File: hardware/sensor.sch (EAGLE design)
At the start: 39 parts, among them IC1 BN055, IC2 BME280, J1 MICRO_USB_B_HIROSE_ZX62-B-5PA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, SW1 TVAF06-A020B-R, U2 NJM12888F, X1 FA-238

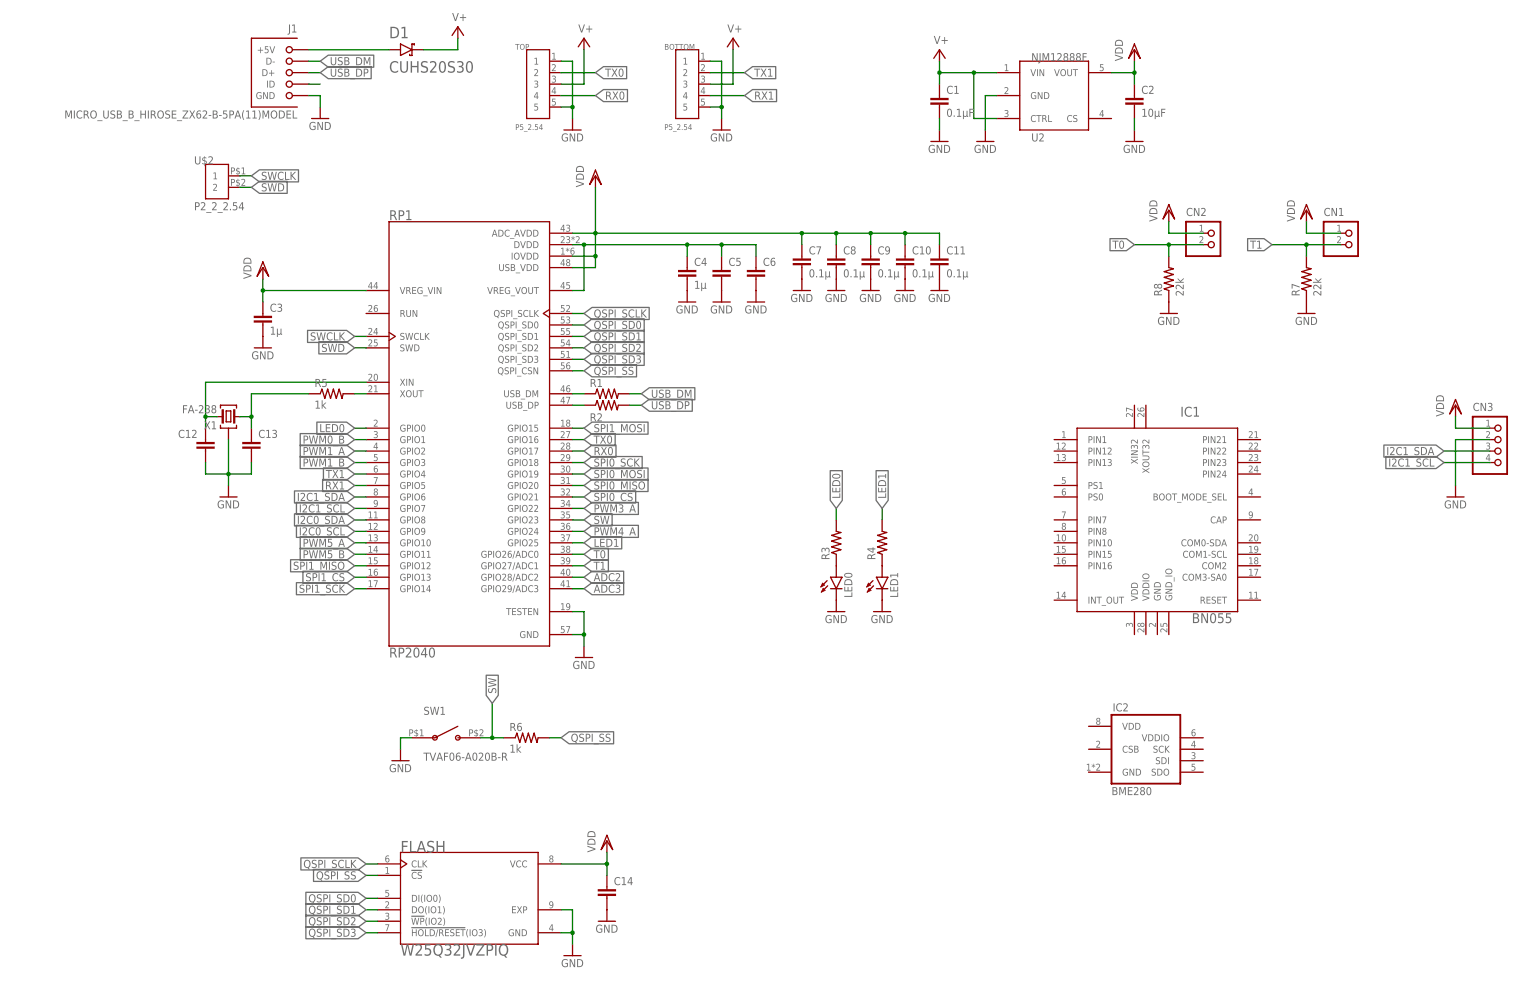
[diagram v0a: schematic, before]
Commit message: センサーの基盤完了しました。エラー処理とか諸々終わってないので年末年始で頑張ります。抵抗値とかなにも入力してなかったのでしばらくかかりそうです。
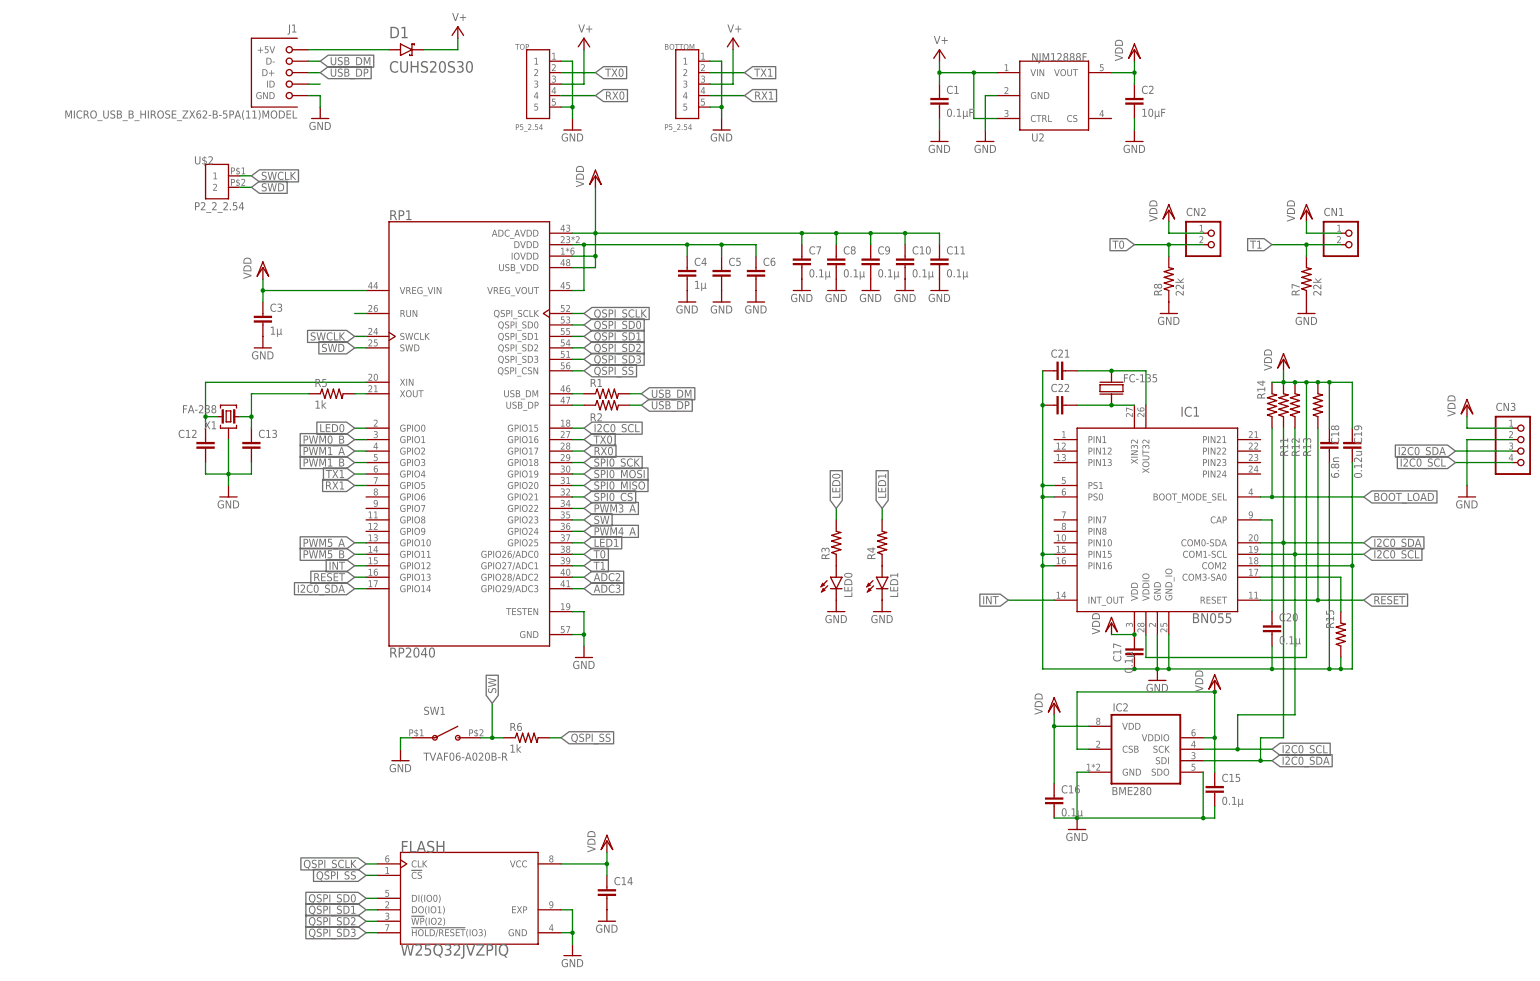
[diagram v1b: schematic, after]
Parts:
- added C15, C16, C17, C20: 0.1µ, rcl:C-EUC0402
- added C18: 6.8n, rcl:C-EUC0402
- added C19: 0.12u, rcl:C-EUC0402
- added C21, C22: (no value), rcl:C-EUC0402
- added FC-135: FC-135, tere:FC-135
- added R11, R12, R13, R14, R15: (no value), rcl:R-US_R0402
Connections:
- removed net I2C1_SCL: CN3.4, RP1.GPIO7
- removed net I2C1_SDA: CN3.3, RP1.GPIO6
- removed net SPI1_CS: RP1.GPIO13
- removed net SPI1_MISO: RP1.GPIO12
- removed net SPI1_MOSI: RP1.GPIO15
- removed net SPI1_SCK: RP1.GPIO14
- new net BOOT_LOAD: IC1.BOOT_MODE_SEL, R14.1
- new net INT: IC1.INT_OUT, RP1.GPIO12
- new net N$1: C20.1, IC1.CAP
- new net N$10: IC1.COM3-SA0, R15.2
- new net N$15: RP1.RUN
- new net N$3: C22.2, FC-135.P$2, IC1.XIN32
- new net N$4: C21.2, FC-135.P$1, IC1.XOUT32
- new net RESET: IC1.RESET, R13.1, RP1.GPIO13
- net GND: now also C15.2, C16.2, C17.2, C18.2, C19.2, C20.2, C21.1, C22.1, IC1.COM2, IC1.GND, IC1.GND_IO, IC1.PIN15, IC1.PIN16, IC1.PS0, IC1.PS1, IC2.GND, IC2.SDO, R15.1
- net I2C0_SCL: now also CN3.4, IC1.COM1-SCL, IC2.SCK, R12.1, RP1.GPIO15; no longer RP1.GPIO9
- net I2C0_SDA: now also CN3.3, IC1.COM0-SDA, IC2.SDI, R11.1, RP1.GPIO14; no longer RP1.GPIO8
- net VDD: now also C15.1, C16.1, C17.1, C18.1, C19.1, IC1.VDD, IC1.VDDIO, IC2.CSB, IC2.VDD, IC2.VDDIO, R11.2, R12.2, R13.2, R14.2
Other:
- moved on the sheet: CN3

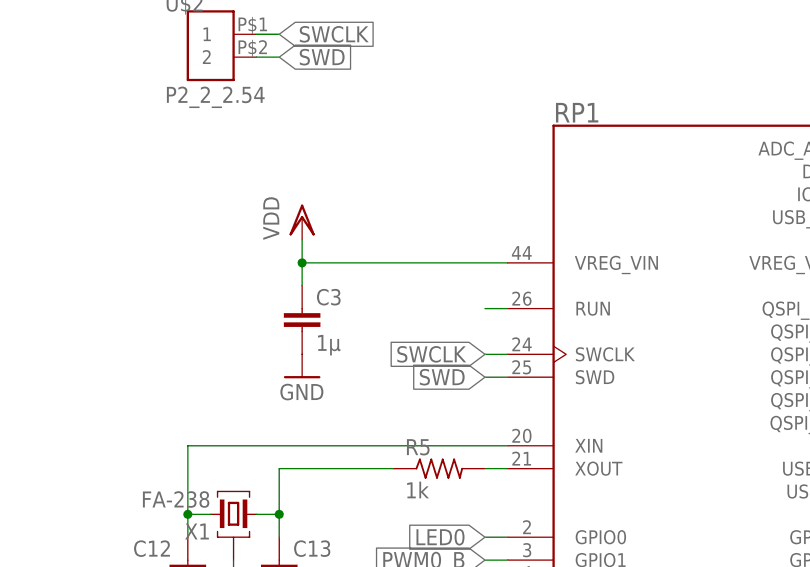
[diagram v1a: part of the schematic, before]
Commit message: べたGND前です。esp32のschはノータッチなのでここに上がってないです。よろしくお願いします。
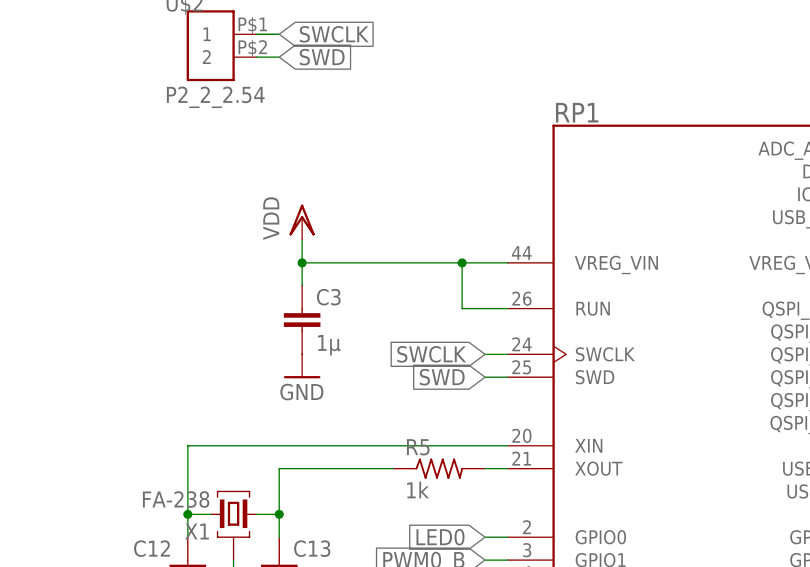
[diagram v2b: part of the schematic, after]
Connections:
- removed net N$15: RP1.RUN
- net VDD: now also RP1.RUN
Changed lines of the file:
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@@
 <segment>
 <pinref part="RP1" gate="G$1" pin="VREG_VIN"/>
-<wire x1="33.02" y1="127" x2="10.16" y2="127" width="0.1524" layer="91"/>
+<wire x1="33.02" y1="127" x2="27.94" y2="127" width="0.1524" layer="91"/>
 <pinref part="C3" gate="G$1" pin="1"/>
+<wire x1="27.94" y1="127" x2="10.16" y2="127" width="0.1524" layer="91"/>
 <wire x1="10.16" y1="127" x2="10.16" y2="124.46" width="0.1524" layer="91"/>
 <wire x1="10.16" y1="127" x2="10.16" y2="129.54" width="0.1524" layer="91"/>
 <junction x="10.16" y="127"/>
 <pinref part="VDD8" gate="G$1" pin="VDD"/>
+<pinref part="RP1" gate="G$1" pin="RUN"/>
+<wire x1="33.02" y1="121.92" x2="27.94" y2="121.92" width="0.1524" layer="91"/>
+<wire x1="27.94" y1="121.92" x2="27.94" y2="127" width="0.1524" layer="91"/>
+<junction x="27.94" y="127"/>
 </segment>
 <segment>
@@
 </segment>
 </net>
-<net name="N$15" class="0">
-<segment>
-<pinref part="RP1" gate="G$1" pin="RUN"/>
-<wire x1="33.02" y1="121.92" x2="30.48" y2="121.92" width="0.1524" layer="91"/>
-</segment>
-</net>

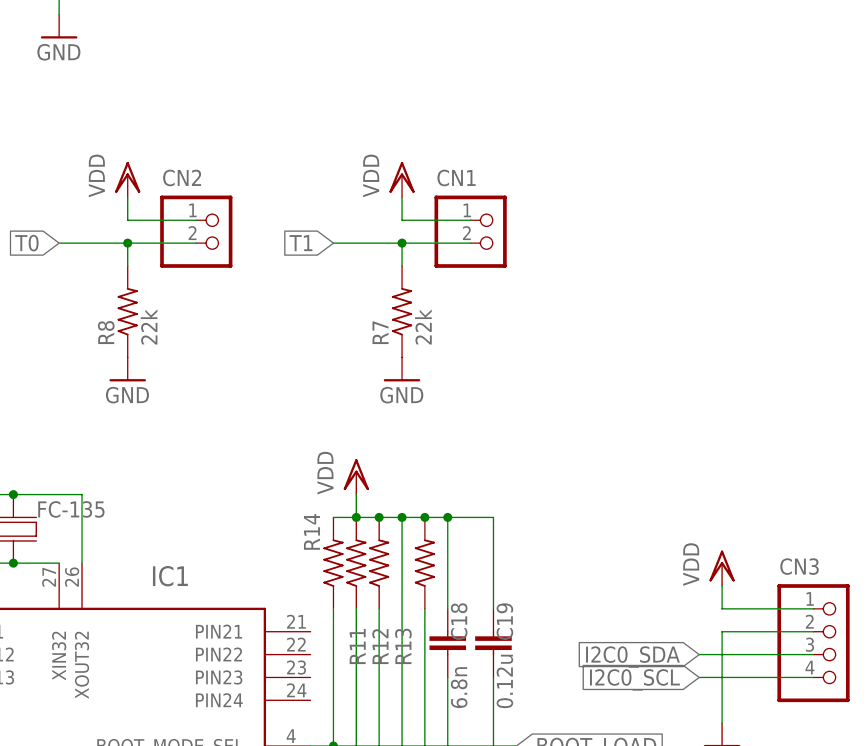
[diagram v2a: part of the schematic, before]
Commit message: シルクを調整
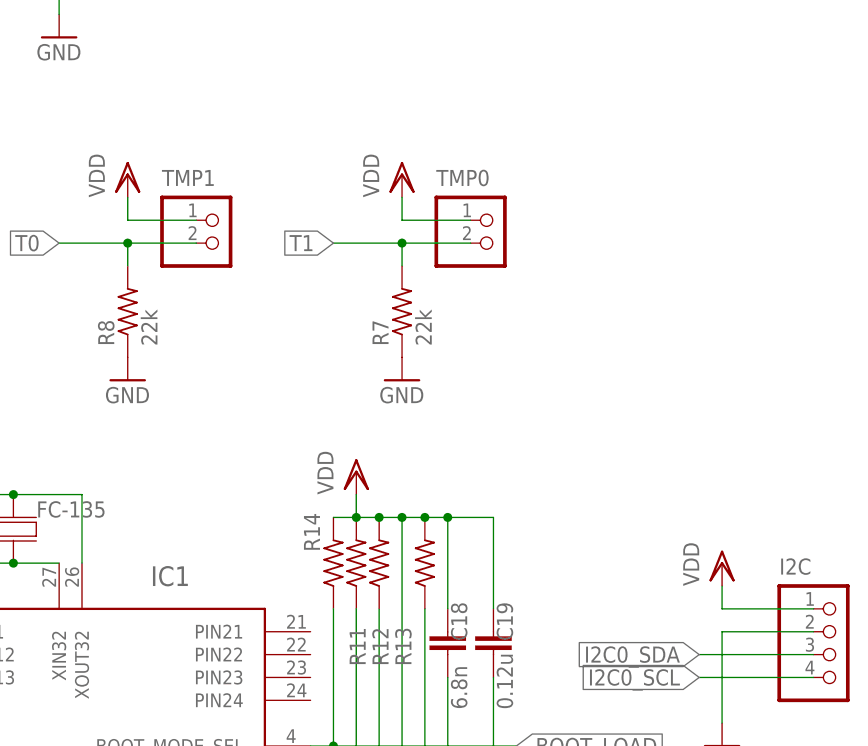
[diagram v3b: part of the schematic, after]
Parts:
- renumbered CN1 to TMP0, CN2 to TMP1, CN3 to I2C
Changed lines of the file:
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@@
 <part name="R7" library="rcl" library_urn="urn:adsk.eagle:library:334" deviceset="R-US_" device="R0402" package3d_urn="urn:adsk.eagle:package:23547/3" value="22k"/>
 <part name="GND1" library="supply1" library_urn="urn:adsk.eagle:library:371" deviceset="GND" device=""/>
-<part name="CN1" library="jst-ph" deviceset="S2B-PH-*" device="K-S"/>
+<part name="TMP0" library="jst-ph" deviceset="S2B-PH-*" device="K-S"/>
 <part name="VDD1" library="supply1" library_urn="urn:adsk.eagle:library:371" deviceset="VDD" device=""/>
 <part name="R8" library="rcl" library_urn="urn:adsk.eagle:library:334" deviceset="R-US_" device="R0402" package3d_urn="urn:adsk.eagle:package:23547/3" value="22k"/>
 <part name="GND2" library="supply1" library_urn="urn:adsk.eagle:library:371" deviceset="GND" device=""/>
-<part name="CN2" library="jst-ph" deviceset="S2B-PH-*" device="K-S"/>
+<part name="TMP1" library="jst-ph" deviceset="S2B-PH-*" device="K-S"/>
 <part name="VDD2" library="supply1" library_urn="urn:adsk.eagle:library:371" deviceset="VDD" device=""/>
-<part name="CN3" library="jst-ph" deviceset="B4B-PH-*" device="K-S"/>
+<part name="I2C" library="jst-ph" deviceset="B4B-PH-*" device="K-S"/>
 <part name="GND3" library="supply1" library_urn="urn:adsk.eagle:library:371" deviceset="GND" device=""/>
 <part name="VDD3" library="supply1" library_urn="urn:adsk.eagle:library:371" deviceset="VDD" device=""/>
@@
 <attribute name="VALUE" x="238.76" y="119.38" size="1.778" layer="96"/>
 </instance>
-<instance part="CN1" gate="G$1" x="248.92" y="139.7" smashed="yes">
+<instance part="TMP0" gate="G$1" x="248.92" y="139.7" smashed="yes">
 <attribute name="NAME" x="245.11" y="143.51" size="1.778" layer="95"/>
 <attribute name="VALUE" x="245.11" y="132.08" size="1.778" layer="96"/>
@@
 <attribute name="VALUE" x="208.28" y="119.38" size="1.778" layer="96"/>
 </instance>
-<instance part="CN2" gate="G$1" x="218.44" y="139.7" smashed="yes">
+<instance part="TMP1" gate="G$1" x="218.44" y="139.7" smashed="yes">
 <attribute name="NAME" x="214.63" y="143.51" size="1.778" layer="95"/>
 <attribute name="VALUE" x="214.63" y="132.08" size="1.778" layer="96"/>
@@
 <attribute name="VALUE" x="208.28" y="142.24" size="1.778" layer="96" rot="R90"/>
 </instance>
-<instance part="CN3" gate="G$1" x="287.02" y="93.98" smashed="yes">
+<instance part="I2C" gate="G$1" x="287.02" y="93.98" smashed="yes">
 <attribute name="NAME" x="283.21" y="100.33" size="1.778" layer="95"/>
 <attribute name="VALUE" x="283.21" y="83.82" size="1.778" layer="96"/>
@@
 </segment>
 <segment>
-<pinref part="CN3" gate="G$1" pin="2"/>
+<pinref part="I2C" gate="G$1" pin="2"/>
 <wire x1="287.02" y1="93.98" x2="276.86" y2="93.98" width="0.1524" layer="91"/>
 <wire x1="276.86" y1="93.98" x2="276.86" y2="83.82" width="0.1524" layer="91"/>
@@
 <wire x1="248.92" y1="139.7" x2="241.3" y2="139.7" width="0.1524" layer="91"/>
 <wire x1="241.3" y1="139.7" x2="241.3" y2="142.24" width="0.1524" layer="91"/>
-<pinref part="CN1" gate="G$1" pin="1"/>
+<pinref part="TMP0" gate="G$1" pin="1"/>
 <pinref part="VDD1" gate="G$1" pin="VDD"/>
 </segment>
@@
 <wire x1="218.44" y1="139.7" x2="210.82" y2="139.7" width="0.1524" layer="91"/>
 <wire x1="210.82" y1="139.7" x2="210.82" y2="142.24" width="0.1524" layer="91"/>
-<pinref part="CN2" gate="G$1" pin="1"/>
+<pinref part="TMP1" gate="G$1" pin="1"/>
 <pinref part="VDD2" gate="G$1" pin="VDD"/>
 </segment>
 <segment>
-<pinref part="CN3" gate="G$1" pin="1"/>
+<pinref part="I2C" gate="G$1" pin="1"/>
 <wire x1="287.02" y1="96.52" x2="276.86" y2="96.52" width="0.1524" layer="91"/>
 <wire x1="276.86" y1="96.52" x2="276.86" y2="99.06" width="0.1524" layer="91"/>
@@
 <net name="I2C0_SDA" class="0">
 <segment>
-<pinref part="CN3" gate="G$1" pin="3"/>
+<pinref part="I2C" gate="G$1" pin="3"/>
 <wire x1="287.02" y1="91.44" x2="274.32" y2="91.44" width="0.1524" layer="91"/>
 <label x="274.32" y="91.44" size="1.778" layer="95" rot="R180" xref="yes"/>
@@
 <wire x1="241.3" y1="137.16" x2="248.92" y2="137.16" width="0.1524" layer="91"/>
 <junction x="241.3" y="137.16"/>
-<pinref part="CN1" gate="G$1" pin="2"/>
+<pinref part="TMP0" gate="G$1" pin="2"/>
 </segment>
 <segment>
@@
 <wire x1="210.82" y1="137.16" x2="218.44" y2="137.16" width="0.1524" layer="91"/>
 <junction x="210.82" y="137.16"/>
-<pinref part="CN2" gate="G$1" pin="2"/>
+<pinref part="TMP1" gate="G$1" pin="2"/>
 </segment>
 <segment>
@@
 <net name="I2C0_SCL" class="0">
 <segment>
-<pinref part="CN3" gate="G$1" pin="4"/>
+<pinref part="I2C" gate="G$1" pin="4"/>
 <wire x1="287.02" y1="88.9" x2="274.32" y2="88.9" width="0.1524" layer="91"/>
 <label x="274.32" y="88.9" size="1.778" layer="95" rot="R180" xref="yes"/>
